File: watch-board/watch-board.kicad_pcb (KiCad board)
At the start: 2 copper layers, 34 x 34 mm, 64 parts, among them J1 Conn_PAD, J2 Conn_PAD, J3 Conn_PAD, J4 Conn_PAD, J5 Conn_PAD, Q1 Phototransistor_ALS-PT19-315C, Q2 Phototransistor_ALS-PT19-315C, Q3 Transistor_MMBT3904-TP, U1 Display-Driver_PCA8561ANH, U2 Regulator_BQ25504, U3 Regulator_LTC3531-3, U4 MCU_STM32L051K8Ux

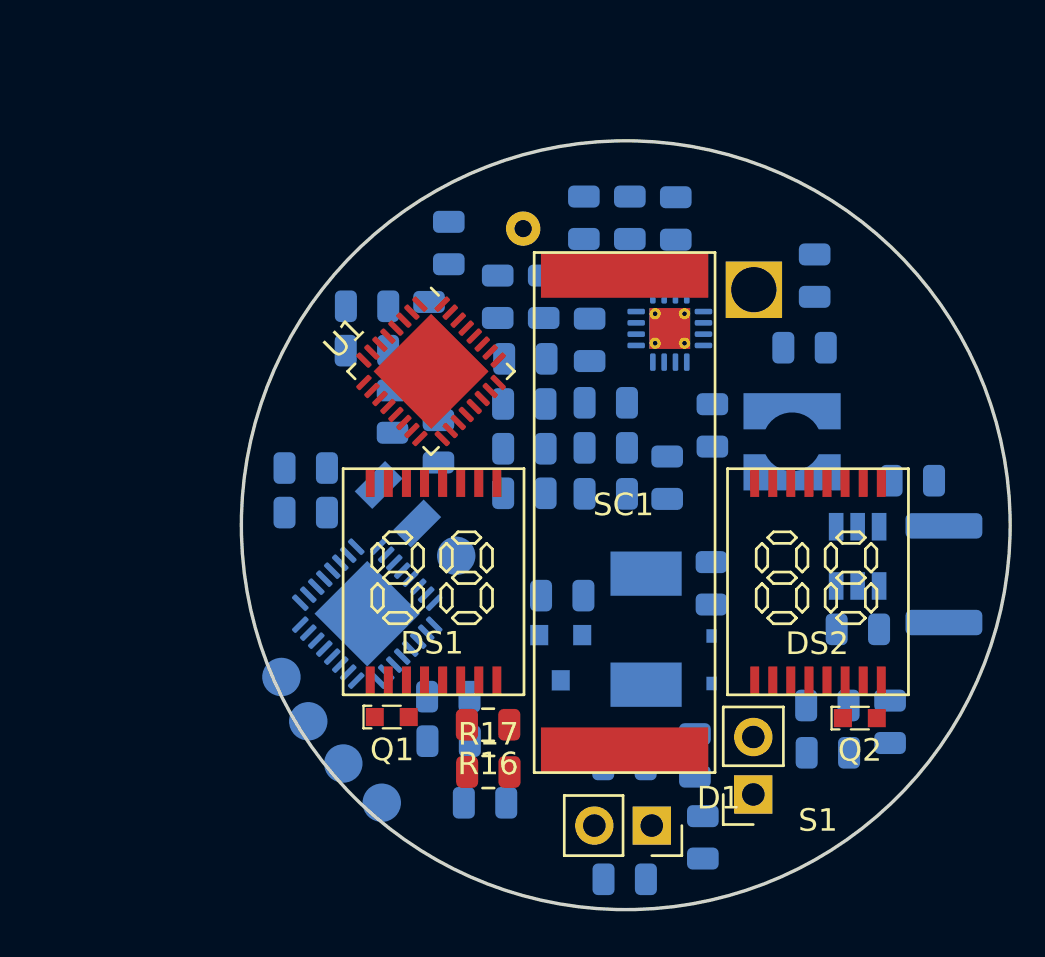
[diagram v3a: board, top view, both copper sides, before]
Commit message: starting layout. connected LCDs
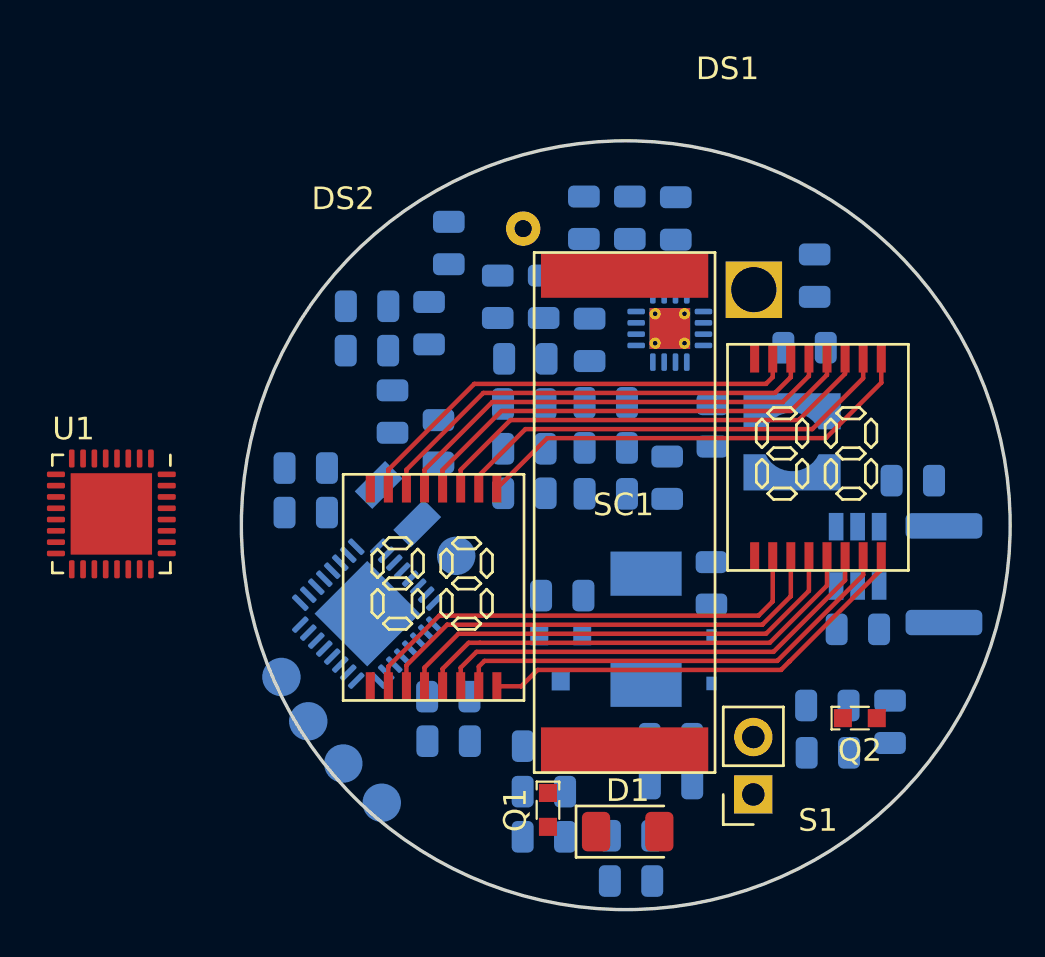
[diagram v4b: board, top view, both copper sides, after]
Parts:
- D1: value LED_WP710A10LSECK-J4 -> LED_APTD3216LSURCK; footprint Connector_PinSocket_2.54mm:PinSocket_1x02_P2.54mm_Vertical -> LED_SMD:LED_1206_3216Metric
- R16, R17: moved to B.Cu
- moved DS1 17.9 mm to (144.5, 92.0)
- moved DS2 17.0 mm to (127.5, 97.8)
- moved U1 15.5 mm to (117.2, 99.5), turned to 270 degrees
- moved Q1 8.04 mm to (136.6, 112.6), turned to 270 degrees
- moved R15 5.16 mm to (140.2, 115.7)
- moved C18 3.00 mm to (136.4, 113.8), turned to 0 degrees
- moved R14 2.76 mm to (142.0, 111.4), turned to 180 degrees
- moved R16 2.65 mm to (136.4, 109.8), turned to 180 degrees
- moved R17 2.61 mm to (136.4, 111.8)
- moved R22 1.95 mm to (140.2, 113.7), turned to 0 degrees
- moved R13 1.29 mm to (142.0, 109.4), turned to 180 degrees
- moved D1 1.10 mm to (140.1, 113.6), turned to 0 degrees
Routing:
- net /1G: track 0.00 -> 21.1 mm
- net /1F: track 0.00 -> 21.0 mm
- net /1E: track 0.00 -> 20.8 mm
- net /1D: track 0.00 -> 20.6 mm
- net /1C: track 0.00 -> 20.5 mm
- net /1B: track 0.00 -> 20.4 mm
- net /2B: track 0.00 -> 20.3 mm
- net /2A: track 0.00 -> 20.3 mm
- net /2C: track 0.00 -> 20.3 mm
- net /2D: track 0.00 -> 20.3 mm
- net /2E: track 0.00 -> 20.3 mm
- net /2F: track 0.00 -> 20.2 mm
- net /2G: track 0.00 -> 20.0 mm
- net /1A: track 0.00 -> 19.8 mm

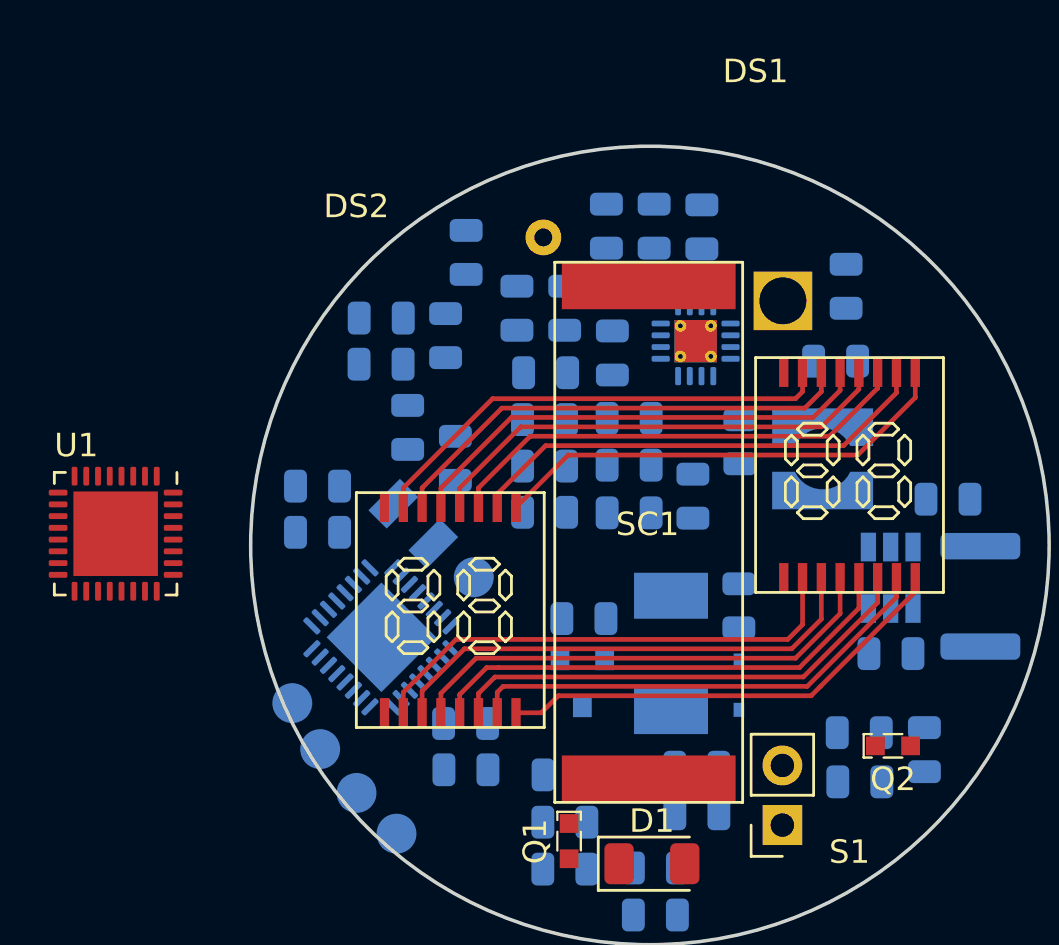
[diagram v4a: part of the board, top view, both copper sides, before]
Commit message: final LCD placement
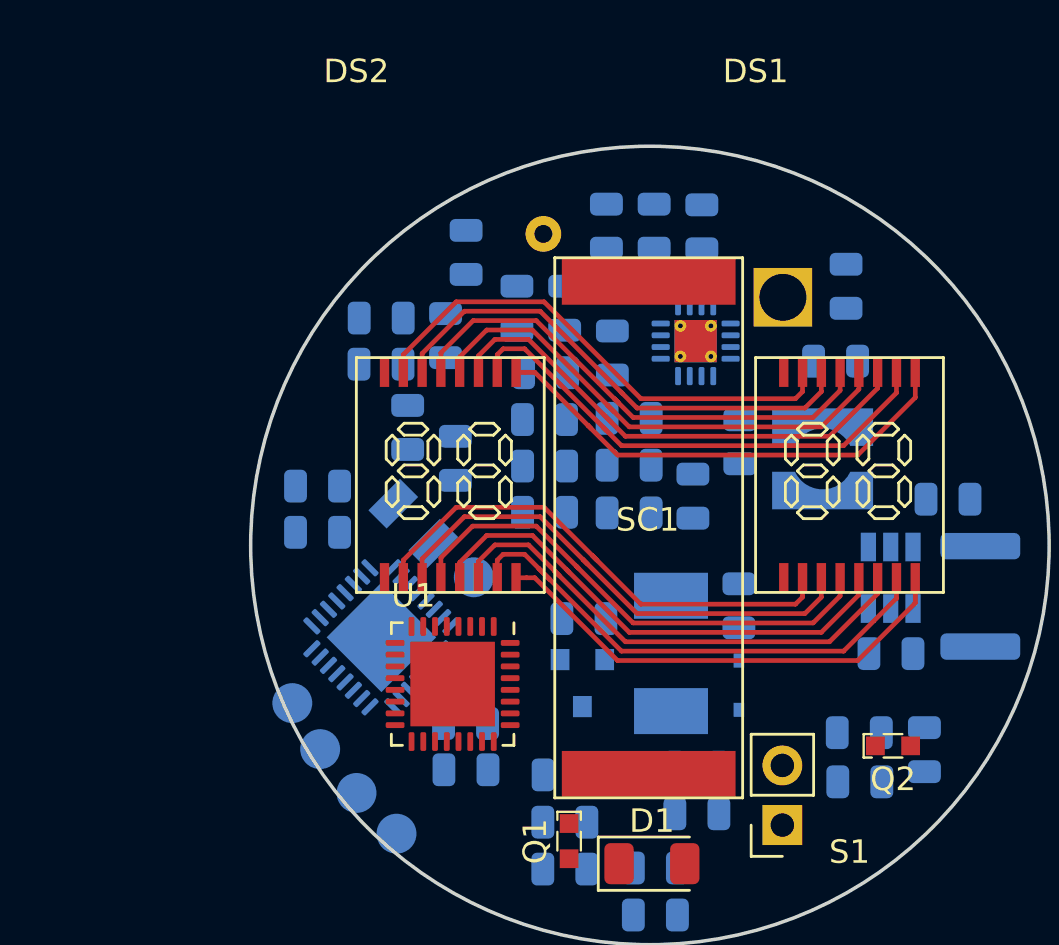
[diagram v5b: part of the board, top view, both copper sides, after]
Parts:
- moved U1 15.7 mm to (131.6, 105.9)
- moved DS2 5.75 mm to (127.5, 92.0)
- moved SC1 0.19 mm to (139.9, 99.2)
- moved BT1 0.15 mm to (145.7, 89.4)
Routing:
- net /1B: track 20.4 -> 22.0 mm
- net /1A: track 19.8 -> 21.2 mm
- net /2E: track 20.3 -> 21.6 mm
- net /2F: track 20.2 -> 21.6 mm
- net /2D: track 20.3 -> 21.6 mm
- net /2C: track 20.3 -> 21.6 mm
- net /2B: track 20.3 -> 21.4 mm
- net /1C: track 20.5 -> 21.5 mm
- net /2A: track 20.3 -> 21.3 mm
- net /2G: track 20.0 -> 20.8 mm
- net /1D: track 20.6 -> 21.3 mm
- net /1E: track 20.8 -> 21.5 mm
- net /1F: track 21.0 -> 21.7 mm
- net /1G: track 21.1 -> 21.6 mm

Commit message: wiring layout for LCDs v2
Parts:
- moved U1 19.7 mm to (113.5, 98.0), turned to 0 degrees
- moved S1 14.3 mm to (159.9, 110.4)
- moved Q1 9.27 mm to (127.6, 115.0)
- moved Q2 7.69 mm to (155.6, 114.2)
- moved DS2 3.31 mm to (127.8, 95.3)
- moved DS1 3.31 mm to (144.8, 95.3)
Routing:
- net /1B: track 22.0 -> 21.5 mm

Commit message: LCDs placed for best wiring
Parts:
- moved U1 20.0 mm to (132.8, 92.4), turned to 270 degrees
- moved Q2 12.2 mm to (143.5, 112.6), turned to 90 degrees
- moved Q1 9.27 mm to (136.6, 112.6)
- moved S1 5.56 mm to (159.7, 116.0)
- moved DS2 1.62 mm to (127.5, 96.9)
- moved DS1 1.62 mm to (144.5, 96.9)
- moved SC1 0.10 mm to (140.0, 99.3)
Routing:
- net /1B: track 21.5 -> 0.00 mm
- net /1E: track 21.4 -> 0.00 mm
- net /1F: track 21.4 -> 0.00 mm
- net /1G: track 21.3 -> 0.00 mm
- net /1C: track 21.2 -> 0.00 mm
- net /1D: track 21.2 -> 0.00 mm
- net /1A: track 21.2 -> 0.00 mm
- net /2G: track 20.8 -> 0.00 mm
- net /2F: track 21.6 -> 2.45 mm
- net /2E: track 21.6 -> 2.76 mm
- net /2D: track 21.6 -> 3.31 mm
- net /2C: track 21.6 -> 3.58 mm
- net /2B: track 21.4 -> 3.99 mm
- net /2A: track 21.3 -> 4.47 mm

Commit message: LCDs fully wired :)
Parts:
- moved U1 0.20 mm to (132.8, 92.2)
- moved SC1 0.09 mm to (140.0, 99.4)
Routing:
- net /1G: track 0.00 -> 39.2 mm
- net /1F: track 0.00 -> 38.7 mm
- net /1E: track 0.00 -> 38.2 mm
- net /1D: track 0.00 -> 37.5 mm
- net /1B: track 0.00 -> 37.0 mm
- net /1C: track 0.00 -> 36.9 mm
- net /COM1: track 0.00 -> 36.8 mm
- net /1A: track 0.00 -> 36.7 mm
- net /COM2: track 0.00 -> 28.1 mm
- net /2G: track 0.00 -> 24.2 mm
- net /2F: track 2.45 -> 24.3 mm
- net /2E: track 2.76 -> 24.4 mm
- net /2D: track 3.31 -> 24.7 mm
- net /2C: track 3.58 -> 25.0 mm
- net /2B: track 3.99 -> 25.1 mm
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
